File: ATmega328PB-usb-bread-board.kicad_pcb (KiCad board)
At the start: 2 copper layers, 60 x 60 mm, 32 parts, among them J1 Conn_01x17, J2 Conn_01x17, J3 USB_B_Micro, J4 AVR-ISP-6, J5 Grove-I2C-connector, J6 Grove-I2C-connector, J7 Grove-I2C-connector, U1 ATmega328PB-MU, U2 CP2102N-A01-GQFN28, U3 LMV358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

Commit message: Update pcb
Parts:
- removed JP1, JP2, JP5, JP6: NC, Jumper:SolderJumper-2_P1.3mm_Bridged_RoundedPad1.0x1.5mm
- removed Y1: Resonator, Crystal:Resonator_SMD_Murata_CSTxExxV-3Pin_3.0x1.1mm
- added C11: 15pf, Capacitor_SMD:C_0603_1608Metric, B.Cu at (138.6, 76.7)
- added C4: 0.1uf, Capacitor_SMD:C_0603_1608Metric, B.Cu at (137.1, 98.9)
- added C5: 4.7uf, Capacitor_SMD:C_0402_1005Metric, B.Cu at (138.2, 100.3)
- added C6: 4.7uf, Capacitor_SMD:C_0402_1005Metric, B.Cu at (140.1, 100.3)
- added C7: 0.1uf, Capacitor_SMD:C_0603_1608Metric, B.Cu at (139.6, 101.7)
- added C9: 0.1uf, Capacitor_SMD:C_0603_1608Metric, B.Cu at (138.5, 71.7)
- added R4: 1k, Resistor_SMD:R_0603_1608Metric, B.Cu at (136.1, 97.3)
- added U5: SiT2001B-MEMS-Clock-Generator, Package_TO_SOT_SMD:SOT-23-5, B.Cu at (138.6, 74.2)
- JP3, JP4: footprint Jumper:SolderJumper-2_P1.3mm_Bridged_RoundedPad1.0x1.5mm -> my-kicad-footprints:SolderJumper-2_P1.3mm_Bridged_RoundedPad1.0x1.5mm
- moved D5 19.4 mm to (133.9, 107.4)
- moved C3 4.30 mm to (132.5, 95.1)
- moved R2 3.98 mm to (132.8, 103.2), turned to 270 degrees
- moved JP3 3.69 mm to (148.7, 96.6)
- moved JP4 3.69 mm to (148.7, 92.9)
- moved R3 3.69 mm to (146.5, 104.3)
- moved U2 3.69 mm to (142.0, 96.4)
- moved U3 3.69 mm to (149.1, 100.8)
- moved D3 3.67 mm to (138.5, 104.7)
- moved D2 3.63 mm to (138.5, 106.7)
- moved D1 3.61 mm to (138.4, 108.7)
- moved R1 1.33 mm to (132.8, 100.0), turned to 270 degrees
- moved C2 0.09 mm to (138.6, 78.2)
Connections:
- J2 pad 16: /avcc -> VCC
- J2 pad 8: /pb6 -> +3V3
- U1 pad 18: /avcc -> VCC
- U1 pad 7: Net-(JP5-Pad1) -> /16MHz
- U1 pad 8: Net-(JP6-Pad1) -> /pb7
- U2 pad 28: Net-(JP2-Pad1) -> /DTR
- U2 pad 6: Net-(D1-Pad1) -> +3V3
- U2 pad 7: Net-(D1-Pad1) -> VCC
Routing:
- net GND: track 495.8 -> 278.2 mm, vias 24 -> 6
- net VCC: track 133.1 -> 206.4 mm, vias 2 -> 1
- net +3V3: track 0.00 -> 41.6 mm, vias 0 -> 1
- net /pb6: track 33.9 -> 0.00 mm, vias 1 -> 0
- net /DTR: track 21.5 -> 49.2 mm, vias 0 -> 1
- net Net-(JP2-Pad1): track 26.3 -> 0.00 mm
- net /pb5: track 98.8 -> 72.9 mm, vias 1 -> 2
- net /pe0: track 49.9 -> 72.7 mm
- net /pc4: track 75.6 -> 96.8 mm, vias 1 -> 0
- net /avcc: track 17.3 -> 0.00 mm
- net /pb3: track 59.9 -> 44.3 mm, vias 0 -> 1
- net Net-(D1-Pad1): track 43.0 -> 27.5 mm
- net /pc6: track 52.2 -> 40.1 mm
- net /pb7: track 35.9 -> 45.6 mm
- net /pd7: track 27.9 -> 36.9 mm, vias 0 -> 1
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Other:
- board text added: "3V3"
- board text removed: "(VCC via jumper)"
- board text removed: "AVCC"
- board text removed: "D20/XTAL1"
- board text removed: "PB6"

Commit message: Update revision to 2020.11
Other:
- board text added: "rev2020.11"
- board text removed: "rev2020.10"

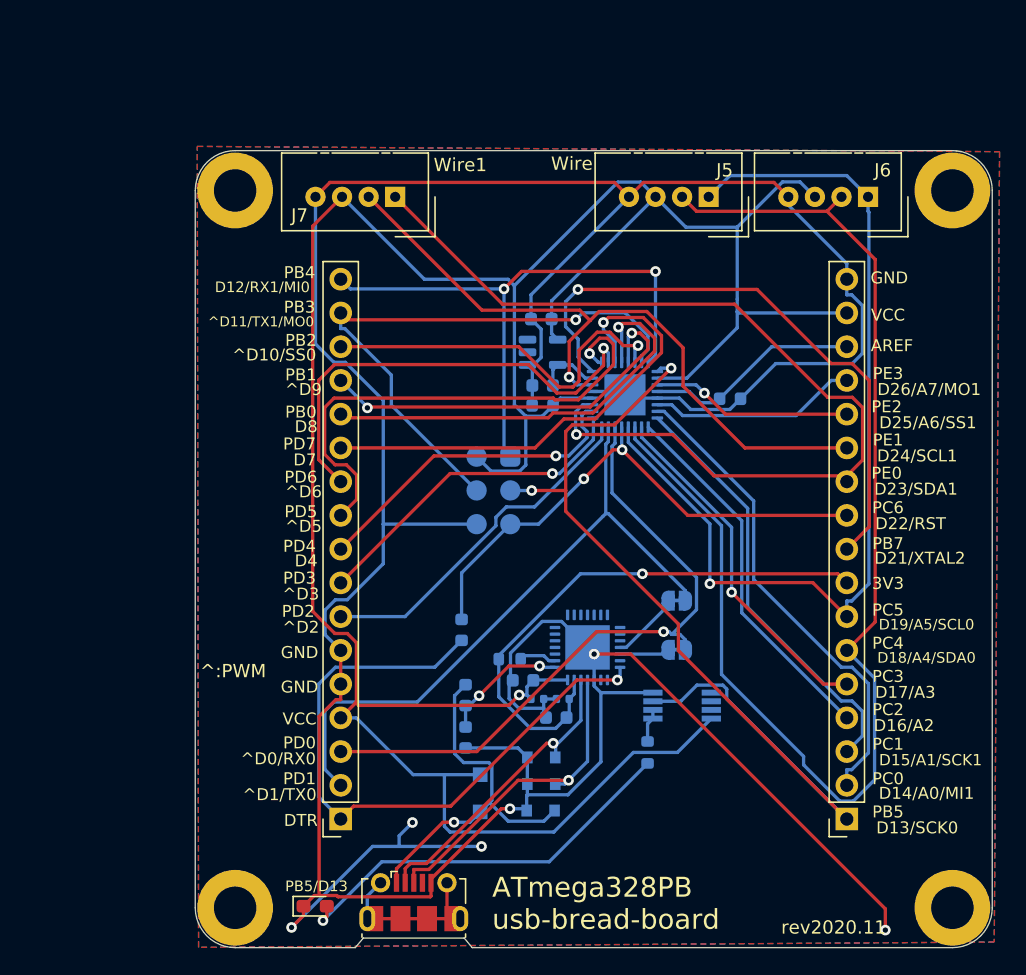
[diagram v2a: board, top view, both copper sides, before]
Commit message: Change zenar and change position of led and usb
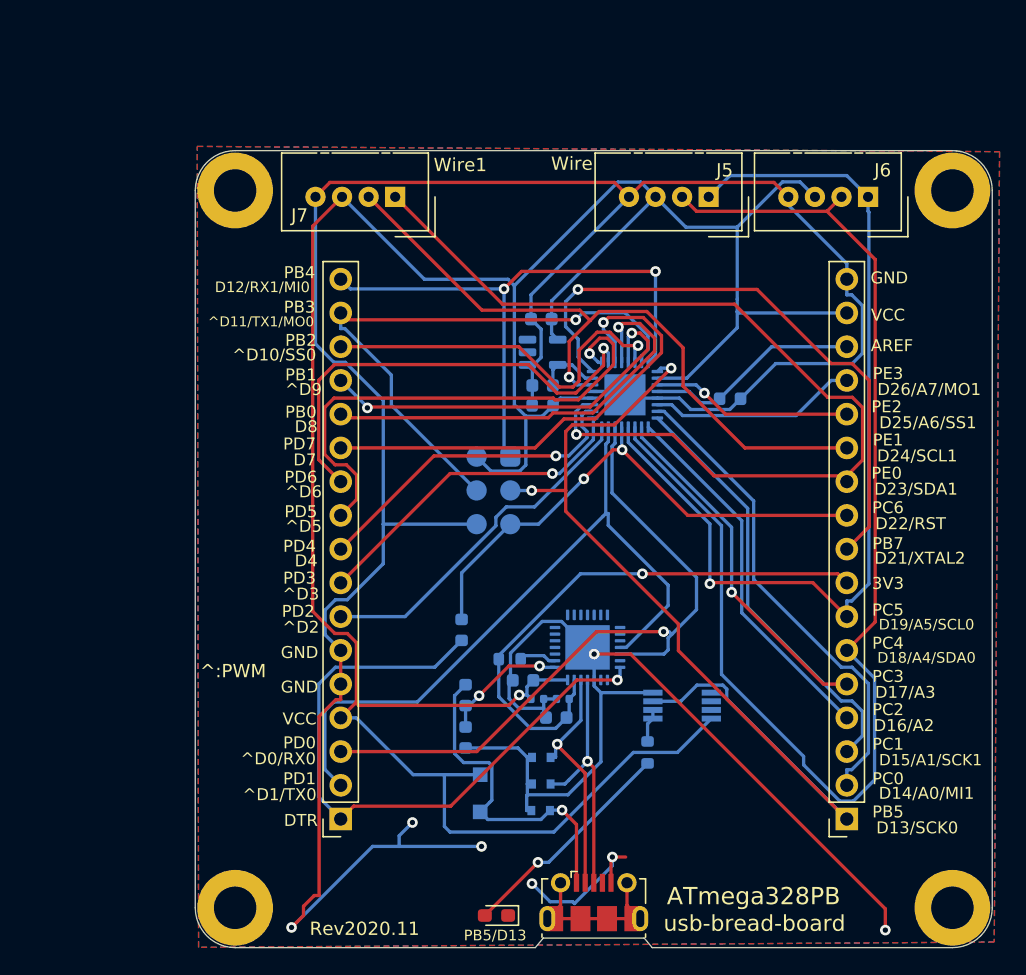
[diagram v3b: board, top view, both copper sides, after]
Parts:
- removed JP3, JP4: NC, my-kicad-footprints:SolderJumper-2_P1.3mm_Bridged_RoundedPad1.0x1.5mm
- D1, D2, D3: footprint my-kicad-footprints:D_UMD2 -> Diode_SMD:D_SOD-523
- R3: value 1k -> 10k
- moved D4 13.7 mm to (135.1, 116.6), turned to 180 degrees
- moved J3 13.5 mm to (142.4, 115.6)
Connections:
- J1 pad 2: /pd1 -> /USB_UART_RX
- J1 pad 3: /pd0 -> /USB_UART_TX
- U1 pad 30: /pd0 -> /USB_UART_TX
- U1 pad 31: /pd1 -> /USB_UART_RX
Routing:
- net /pd0: track 49.9 -> 0.00 mm, vias 1 -> 0
- net /pd1: track 49.3 -> 0.00 mm
- net /USB_UART_TX: track 3.75 -> 52.9 mm, vias 0 -> 1
- net /USB_UART_RX: track 5.29 -> 53.9 mm
- net Net-(D4-Pad2): track 30.5 -> 17.0 mm
- net GND: track 278.2 -> 271.6 mm, vias 6 -> 7
- net Net-(D2-Pad1): track 24.7 -> 18.9 mm
- net Net-(D3-Pad1): track 23.0 -> 18.3 mm
- net Net-(D1-Pad1): track 27.5 -> 25.2 mm
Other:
- outline, holes or cut-outs redrawn
- board text added: "ATmega328PB"
- board text added: "Rev2020.11"
- board text added: "usb-bread-board"
- board text removed: "ATmega328PB usb-bread-board"
- board text removed: "rev2020.11"

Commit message: Use diode array and update holes position as Rev2021.03
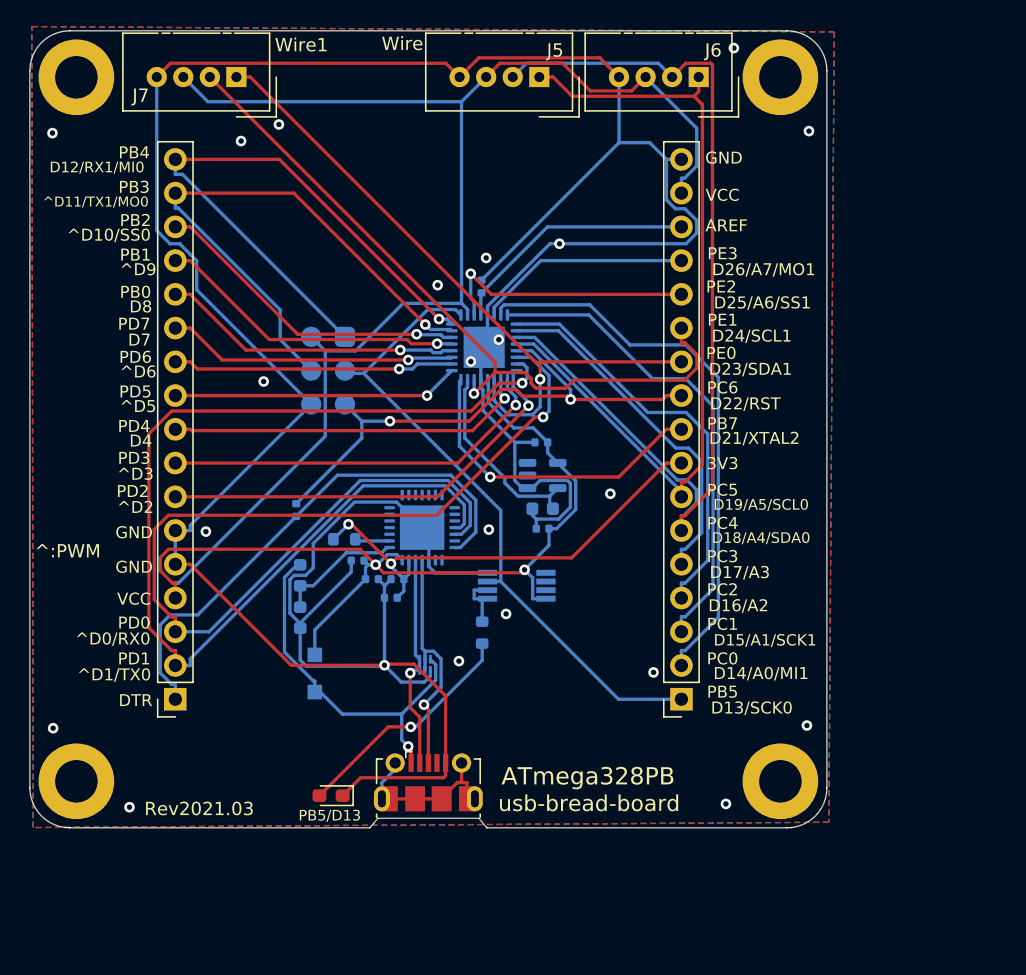
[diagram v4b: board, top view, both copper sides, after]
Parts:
- removed D2, D3: DZ, Diode_SMD:D_SOD-523
- C1, C2, C3, C4, C7, C9: footprint Capacitor_SMD:C_0603_1608Metric -> Capacitor_SMD:C_0402_1005Metric
- D1: value DZ -> Diode_4array_ESDR0502NMUTBG; footprint Diode_SMD:D_SOD-523 -> my-kicad-footprints:OnSemi_UDFN-6_1.2x1.0mm_P0.4mm
- moved C1 20.5 mm to (134.0, 69.2), turned to 90 degrees
- moved REF2 16.1 mm to (156.5, 106.5)
- moved J5 15.6 mm to (138.3, 53.5)
- moved J6 15.6 mm to (150.3, 53.5)
- moved REF3 15.5 mm to (156.5, 53.5)
- moved R1 15.4 mm to (120.3, 91.0)
- moved R2 15.4 mm to (120.3, 94.2)
- moved C4 15.4 mm to (124.7, 89.9)
- moved D5 15.4 mm to (121.5, 98.4)
- moved J1 15.4 mm to (111.0, 100.3)
- moved C3 15.4 mm to (120.0, 86.1)
- moved C6 15.4 mm to (127.7, 91.3)
- moved C7 15.4 mm to (127.2, 92.7)
- moved D4 15.4 mm to (122.7, 107.6)
- moved J4 15.4 mm to (122.5, 75.6)
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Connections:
- D1 pad 1: Net-(D1-Pad1) -> GND
- D1 pad 2: GND -> Net-(D1-Pad2)
- D5 pad 2: Net-(D1-Pad1) -> Net-(D1-Pad6)
- J3 pad 1: Net-(D1-Pad1) -> Net-(D1-Pad6)
- J3 pad 2: Net-(D3-Pad1) -> Net-(D1-Pad3)
- J3 pad 3: Net-(D2-Pad1) -> Net-(D1-Pad2)
- R1 pad 1: Net-(D1-Pad1) -> Net-(D1-Pad6)
- U2 pad 4: Net-(D2-Pad1) -> Net-(D1-Pad2)
- U2 pad 5: Net-(D3-Pad1) -> Net-(D1-Pad3)
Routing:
- net VCC: track 206.4 -> 169.3 mm, vias 1 -> 2
- net Net-(D1-Pad6): track 0.00 -> 28.0 mm, vias 0 -> 1
- net /USB_UART_RX: track 53.9 -> 80.8 mm, vias 0 -> 1
- net /USB_UART_TX: track 52.9 -> 78.4 mm
- net Net-(D1-Pad1): track 25.2 -> 0.00 mm, vias 1 -> 0
- net /pb5: track 72.9 -> 49.2 mm, vias 2 -> 0
- net /pc4: track 96.8 -> 74.5 mm
- net /pb7: track 45.6 -> 24.2 mm
- net /pe0: track 72.7 -> 51.5 mm
- net GND: track 271.6 -> 252.6 mm, vias 7 -> 22
- net Net-(D2-Pad1): track 18.9 -> 0.00 mm, vias 1 -> 0
- net Net-(D1-Pad2): track 0.00 -> 18.4 mm, vias 0 -> 1
- net Net-(D3-Pad1): track 18.3 -> 0.00 mm, vias 1 -> 0
- net /pd5: track 38.7 -> 21.6 mm
- net Net-(D1-Pad3): track 0.00 -> 16.3 mm, vias 0 -> 1
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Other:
- net class Default: clearance 0.2 -> 0.15
- rule trace_clearance: 0.2 -> 0.15
- board text added: "Rev2021.03"
- board text removed: "Rev2020.11"

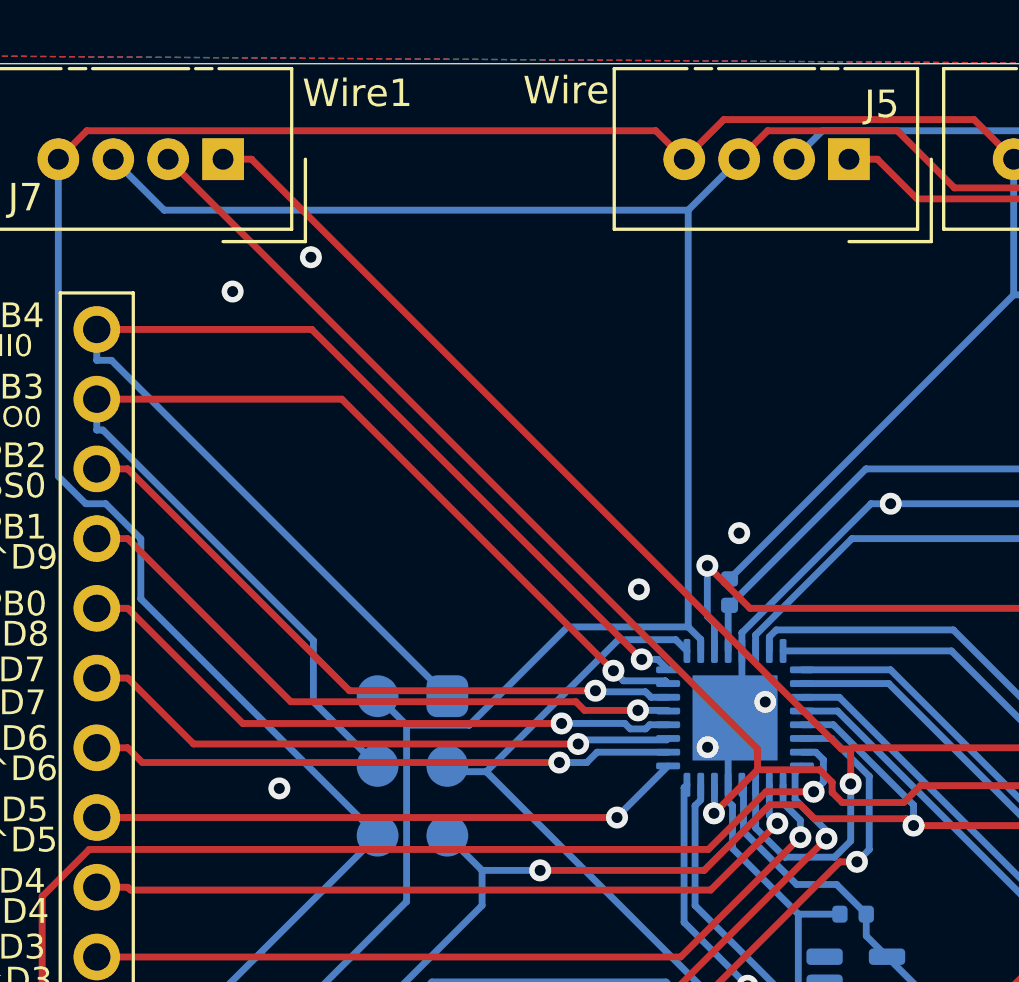
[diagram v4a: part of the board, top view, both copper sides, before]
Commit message: Correct pin asign for Wire1 grove connector
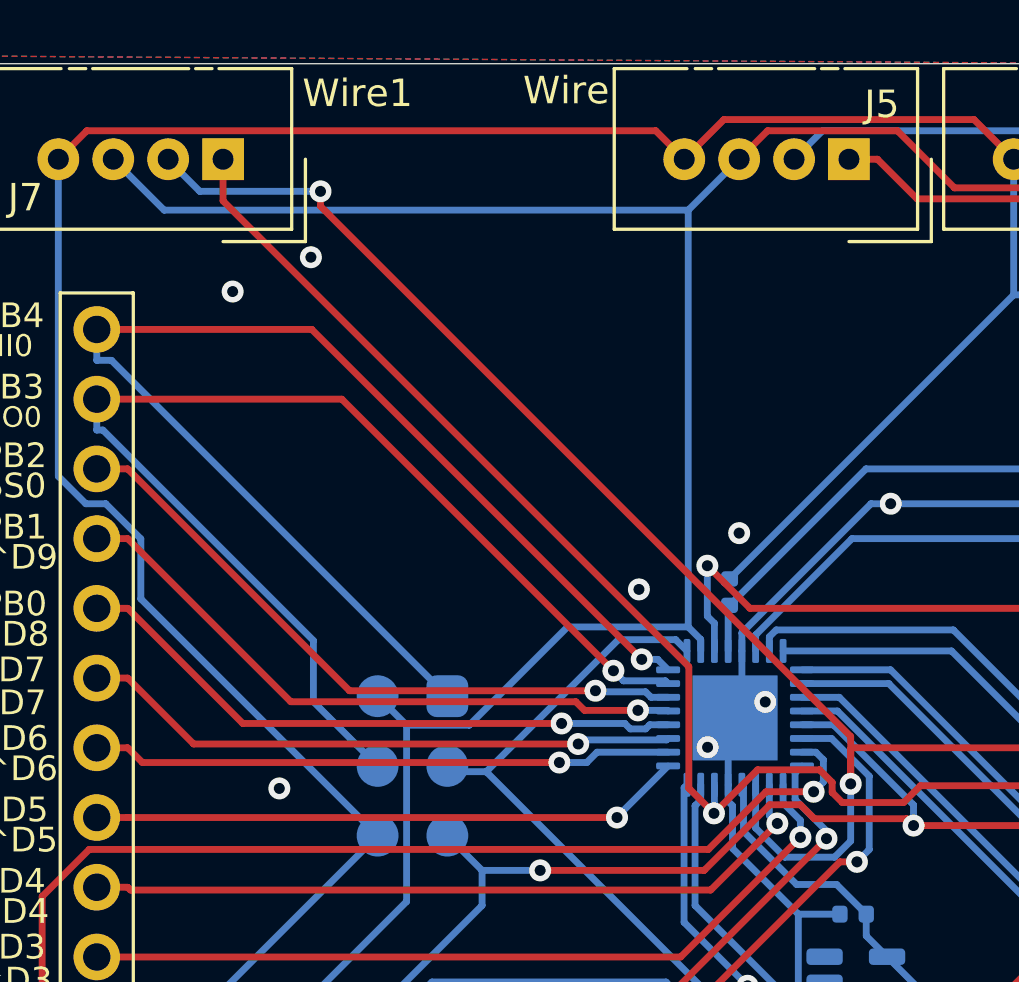
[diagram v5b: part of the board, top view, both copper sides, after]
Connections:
- J7 pad 1: /pe0 -> /pe1
- J7 pad 2: /pe1 -> /pe0
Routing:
- net /pe0: track 51.5 -> 55.4 mm, vias 1 -> 2

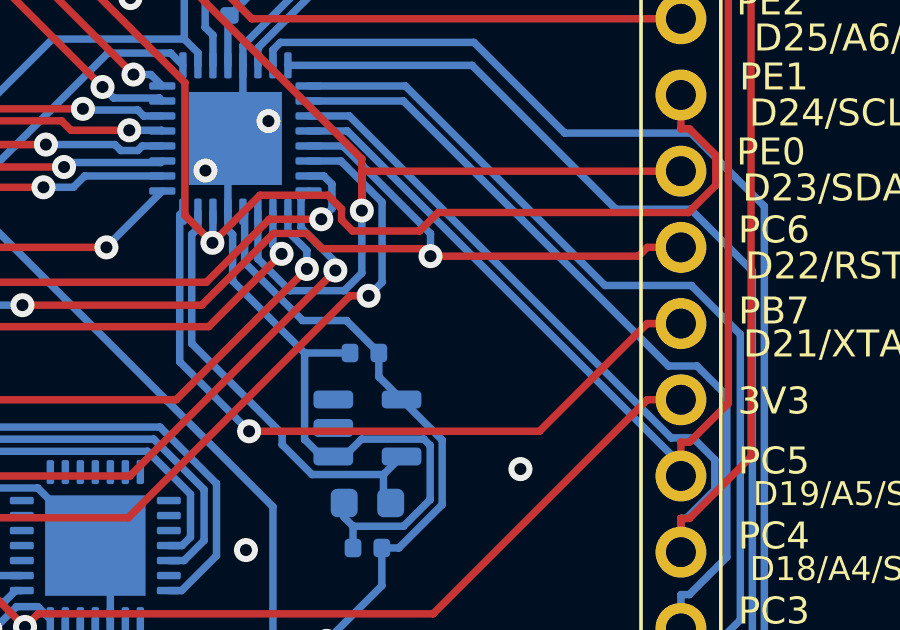
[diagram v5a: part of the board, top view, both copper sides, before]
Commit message: Add pullup resistor to RST
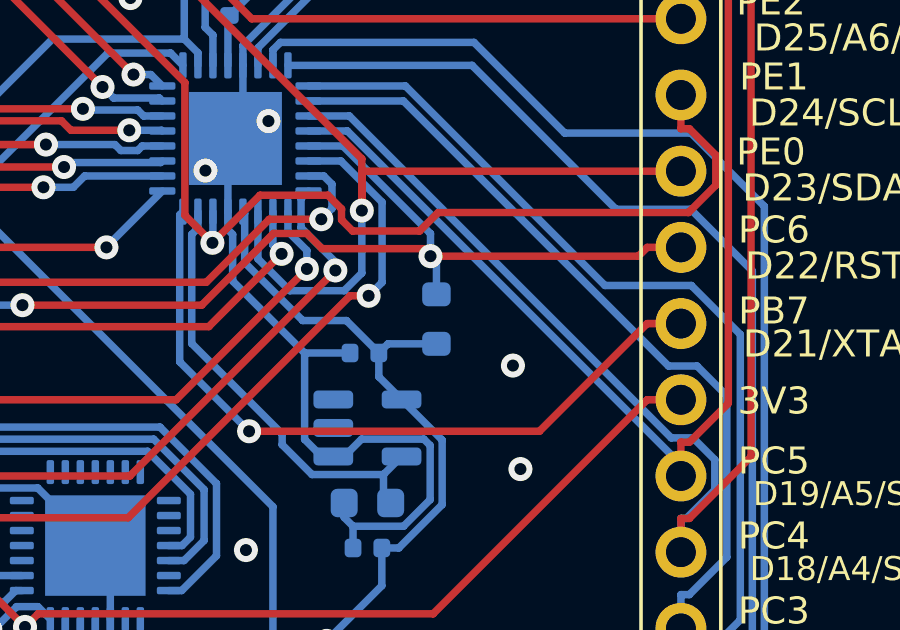
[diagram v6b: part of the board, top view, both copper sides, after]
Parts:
- added R5: 10k, Resistor_SMD:R_0603_1608Metric, B.Cu at (140.9, 79.8)
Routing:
- net VCC: track 169.3 -> 171.3 mm
- net /pc6: track 41.6 -> 42.9 mm
- net GND: vias 22 -> 23

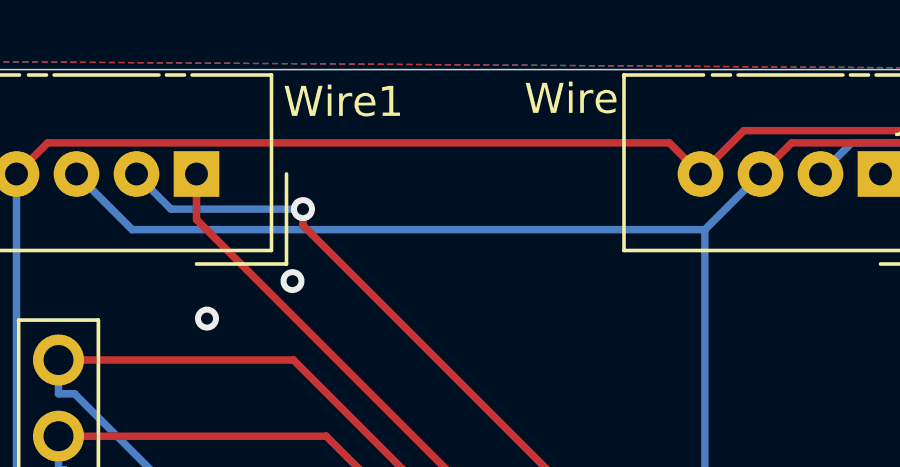
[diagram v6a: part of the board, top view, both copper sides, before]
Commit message: Add labels about pins for Grove connectors
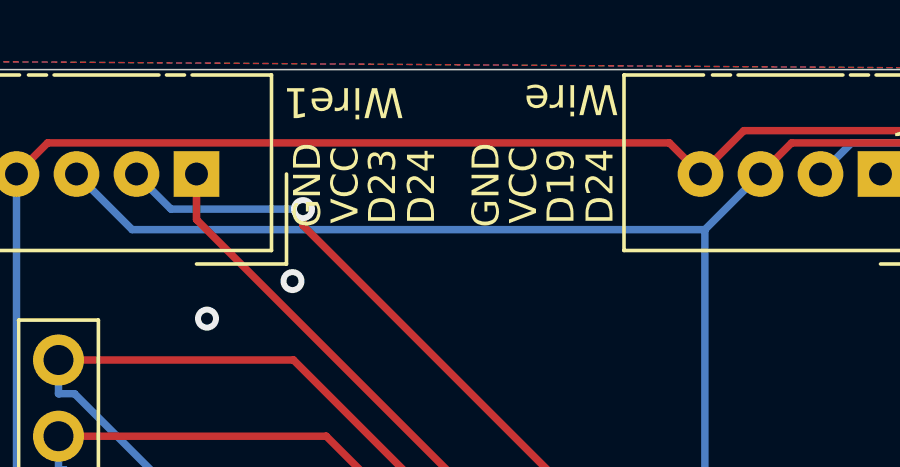
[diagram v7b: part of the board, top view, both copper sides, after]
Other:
- board text added: "D19"
- board text added: "D23"
- board text added: "D24"
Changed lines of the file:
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@@
   (general
     (thickness 1.6)
-    (drawings 82)
+    (drawings 90)
     (tracks 583)
     (zones 0)
@@
     )
   )
+  (gr_text VCC (at 126.45 53.85 90) (layer F.SilkS)
+    (effects (font (size 0.9 0.9) (thickness 0.15)))
+  )
+  (gr_text D19 (at 127.7 53.9 90) (layer F.SilkS)
+    (effects (font (size 0.9 0.9) (thickness 0.15)))
+  )
+  (gr_text D24 (at 129 53.9 90) (layer F.SilkS)
+    (effects (font (size 0.9 0.9) (thickness 0.15)))
+  )
+  (gr_text GND (at 125.2 53.85 90) (layer F.SilkS)
+    (effects (font (size 0.9 0.9) (thickness 0.15)))
+  )
+  (gr_text D24 (at 123.05 53.9 90) (layer F.SilkS)
+    (effects (font (size 0.9 0.9) (thickness 0.15)))
+  )
+  (gr_text D23 (at 121.75 53.9 90) (layer F.SilkS)
+    (effects (font (size 0.9 0.9) (thickness 0.15)))
+  )
+  (gr_text VCC (at 120.5 53.85 90) (layer F.SilkS)
+    (effects (font (size 0.9 0.9) (thickness 0.15)))
+  )
+  (gr_text GND (at 119.25 53.85 90) (layer F.SilkS)
+    (effects (font (size 0.9 0.9) (thickness 0.15)))
+  )
   (dimension 60 (width 0.15) (layer Dwgs.User)
     (gr_text "60.000 mm" (at 165.15 80 270) (layer Dwgs.User)
@@
   (gr_line (start 126.2 109.28) (end 133.8 109.28) (layer Edge.Cuts) (width 0.05))
   (gr_line (start 125.6 110) (end 126.2 109.28) (layer Edge.Cuts) (width 0.05))
-  (gr_text Wire (at 128.05 50.98) (layer F.SilkS)
+  (gr_text Wire (at 128.05 50.98 180) (layer F.SilkS)
     (effects (font (size 1 1) (thickness 0.15)))
   )
-  (gr_text Wire1 (at 120.45 51.08) (layer F.SilkS)
+  (gr_text Wire1 (at 120.45 51.08 180) (layer F.SilkS)
     (effects (font (size 1 1) (thickness 0.15)))
   )
